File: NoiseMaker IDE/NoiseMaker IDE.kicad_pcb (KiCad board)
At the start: 2 copper layers, 60.6 x 72.4 mm, 17 parts, among them J1 IDE_OUT, J2 IDE_IN, J3 PWR, J4 SPK, M1 Mounting, M2 Mounting, M3 Mounting

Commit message: Add test button
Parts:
- added SW1: TEST, switch_cutout:SW_PUSH_6mm, F.Cu at (202.6, 126.4)
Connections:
- A1 pad 19: (no net) -> Net-(A1-Pad19)
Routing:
- net Net-(A1-Pad19): track 0.00 -> 13.7 mm

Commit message: Tweak silkscreen and dimensions
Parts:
- J1: footprint Connector_PinSocket_2.54mm:PinSocket_2x20_P2.54mm_Vertical -> noisemaker:PinSocket_2x20_P2.54mm_Vertical
- moved M2 0.40 mm to (153.7, 135.4)
- moved M3 0.40 mm to (207.1, 135.7)
- moved M1 0.40 mm to (153.7, 70.3)
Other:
- board size 60.6 x 72.4 mm -> 60.6 x 73.2 mm

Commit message: First attempt at sketch
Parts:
- moved JP4 5.08 mm to (196.9, 117.5)
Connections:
- A1 pad 24: (no net) -> Net-(A1-Pad24)
- A1 pad 26: Net-(A1-Pad26) -> (no net)
- JP4 pad 3: Net-(A1-Pad26) -> Net-(A1-Pad24)
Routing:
- net Net-(A1-Pad26): track 3.81 -> 0.00 mm
- net Net-(A1-Pad24): track 0.00 -> 3.81 mm

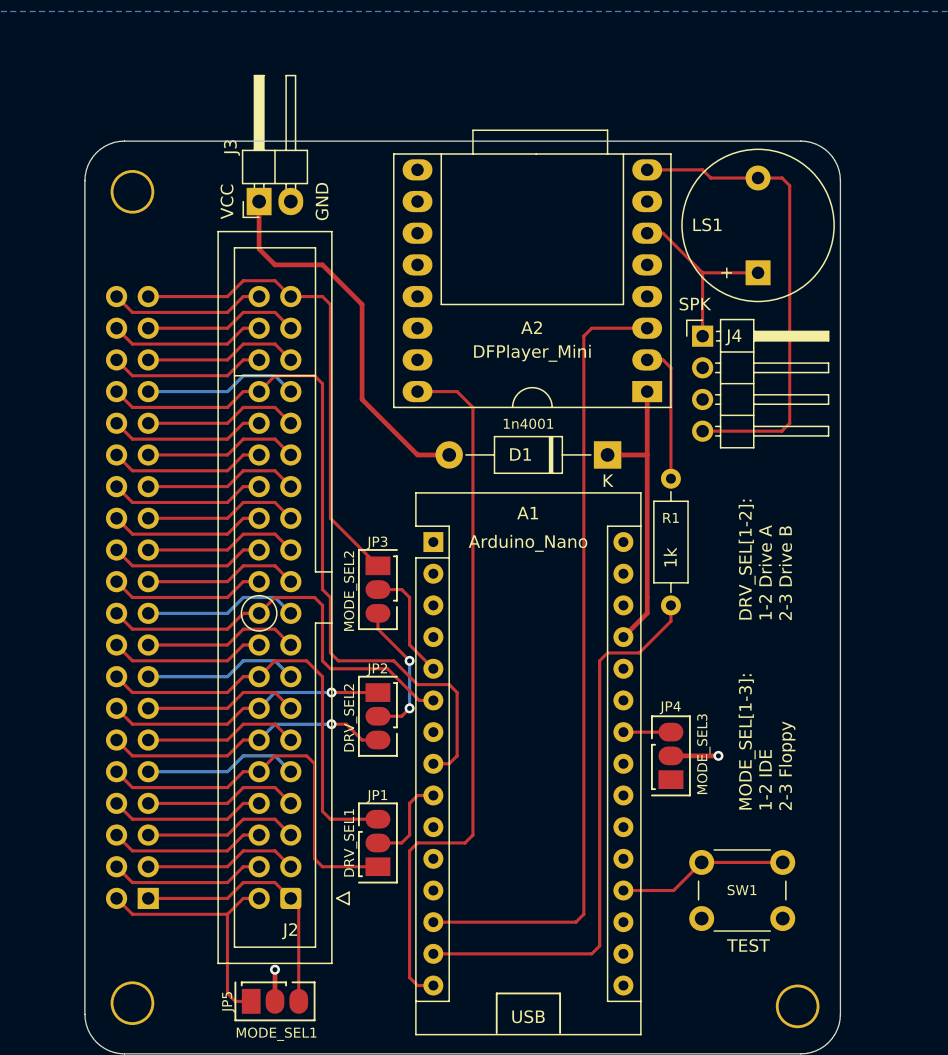
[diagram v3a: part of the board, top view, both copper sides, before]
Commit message: Add proper power connector and more switches
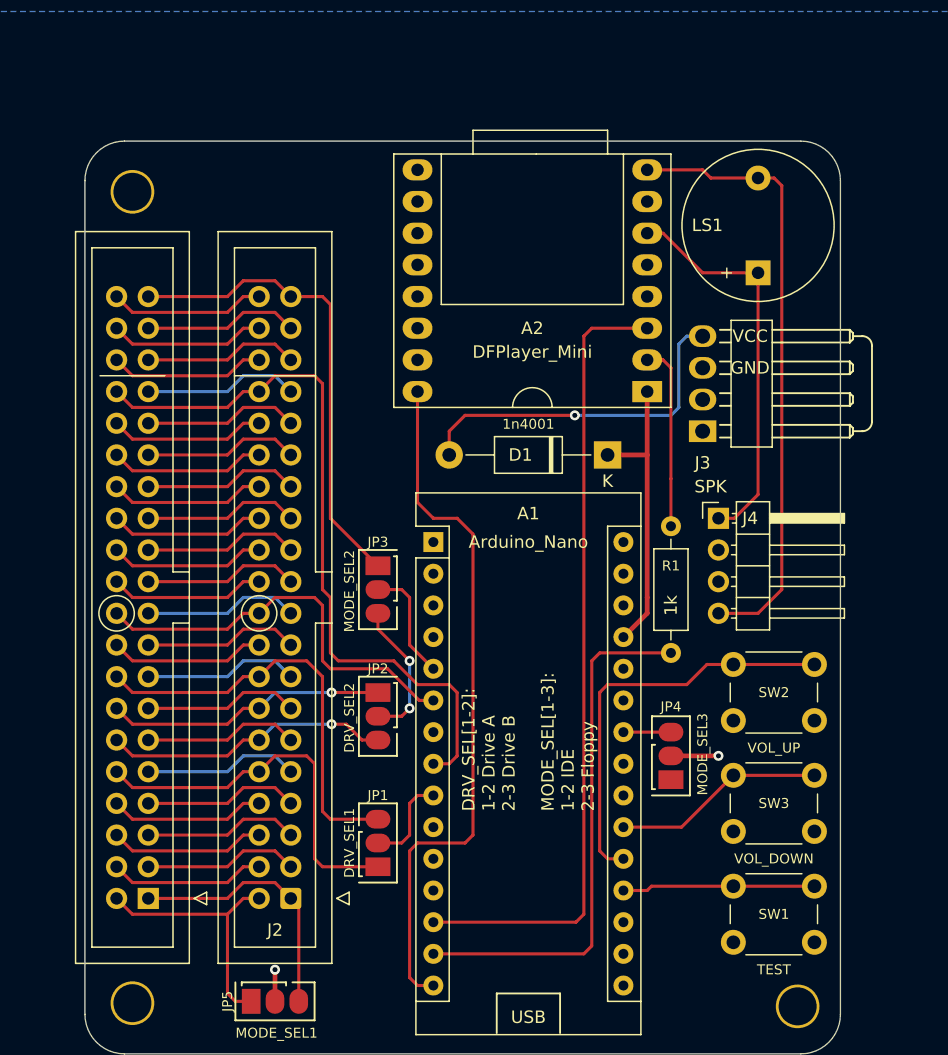
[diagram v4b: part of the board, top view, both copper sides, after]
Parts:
- added SW2: VOL_UP, switch_cutout:SW_PUSH_6mm, F.Cu at (205.2, 110.5)
- added SW3: VOL_DOWN, switch_cutout:SW_PUSH_6mm, F.Cu at (205.2, 119.4)
- J3: footprint noisemaker:Power -> noisemaker:Molex_KK-254_1x04_P2.54mm_Horizontal
- moved J3 40.0 mm to (199.4, 89.5)
- moved J4 14.7 mm to (200.7, 96.5)
- moved R1 3.81 mm to (196.9, 97.2)
- moved SW1 3.18 mm to (205.2, 128.3)
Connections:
- A1 pad 20: (no net) -> Net-(A1-Pad20)
- A1 pad 21: (no net) -> Net-(A1-Pad21)
- J3 pad 1: Net-(D1-Pad2) -> (no net)
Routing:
- net Net-(A1-Pad20): track 0.00 -> 33.0 mm
- net Net-(A1-Pad21): track 0.00 -> 17.0 mm
- net Net-(A2-Pad6): track 15.3 -> 31.9 mm
- net Net-(A2-Pad8): track 38.3 -> 49.6 mm
- net Net-(A2-Pad2): track 11.1 -> 14.9 mm
- net SS_TX: track 44.8 -> 42.4 mm
- net Net-(D1-Pad2): track 30.4 -> 28.4 mm, vias 0 -> 1
- net Net-(A1-Pad19): track 13.7 -> 15.5 mm
- net BUSY: track 57.2 -> 56.5 mm
